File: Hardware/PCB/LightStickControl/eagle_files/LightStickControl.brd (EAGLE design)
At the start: 100 x 80 mm, 3 parts

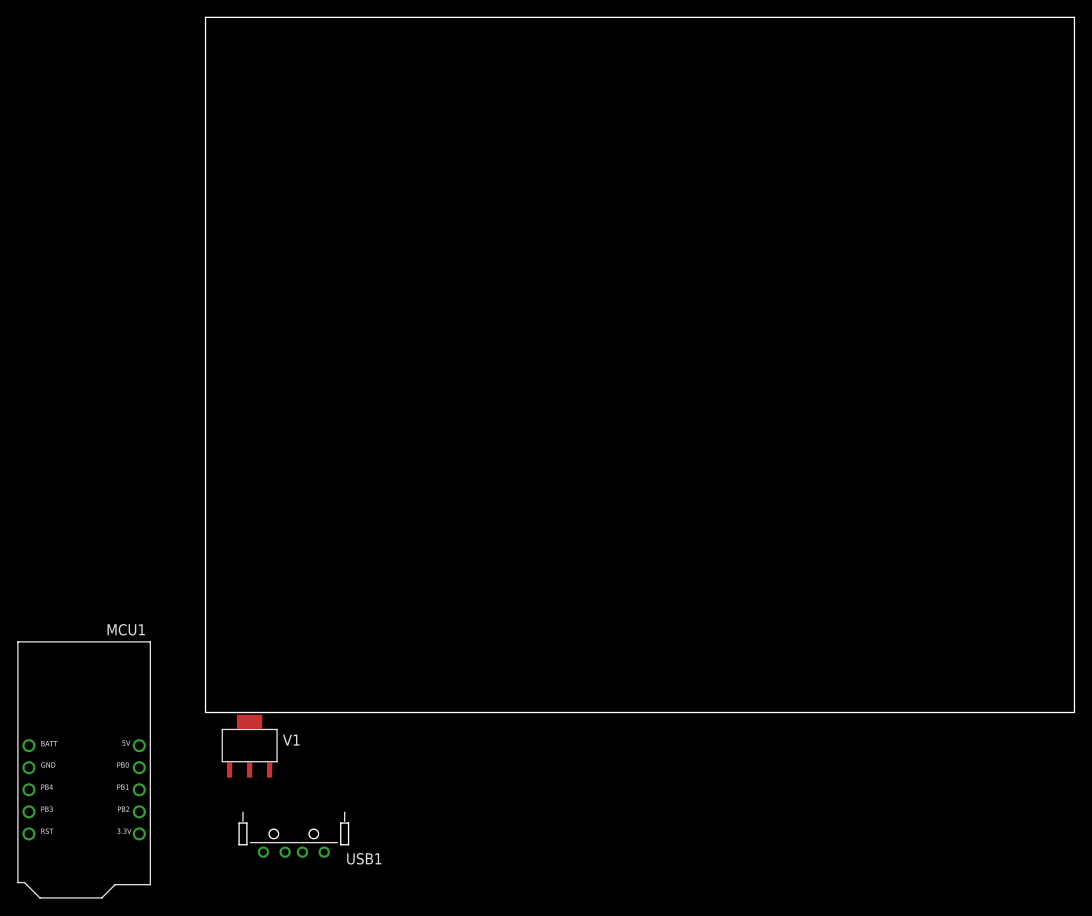
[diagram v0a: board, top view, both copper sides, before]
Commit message: First cut of board layout. Add connectors. Label everything.
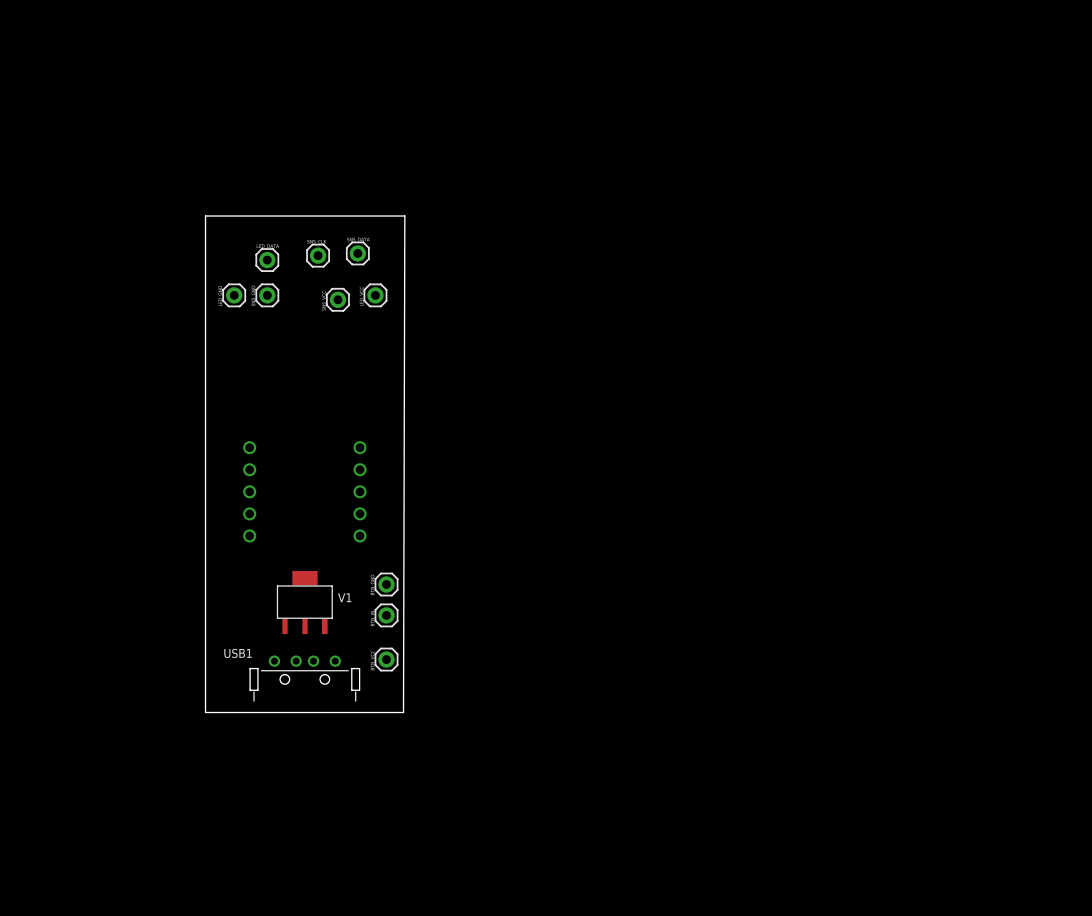
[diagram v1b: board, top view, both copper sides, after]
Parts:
- added BTN_GND, BTN_IN, BTN_VCC, LED_DATA, LED_GND, LED_VCC, SNS_CLK, SNS_DATA, SNS_GND, SNS_VCC: (no value), SparkFun-Connectors:1X01
- moved MCU1 42.7 mm to (11.4, 25.4), flipped to the bottom, turned to 180 degrees
- moved USB1 17.8 mm to (11.4, 3.81), turned to 180 degrees
- moved V1 17.7 mm to (11.4, 12.7)
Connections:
- removed net N$1: USB1.GND, V1.GND
- removed net N$2: USB1.VCC, V1.VIN
- removed net N$3: V1.VOUT2
- removed net N$4: USB1.D+, USB1.D-
- new net BTN_IN: BTN_IN.1, MCU1.PB3
- new net GND: BTN_GND.1, LED_GND.1, MCU1.GND, SNS_GND.1, USB1.D+, USB1.D-, USB1.GND, V1.GND
- new net LED_DATA: LED_DATA.1, MCU1.PB4
- new net LED_VCC: LED_VCC.1, V1.VOUT2
- new net SNS_CLK: MCU1.PB2, SNS_CLK.1
- new net SNS_DATA: MCU1.PB0, SNS_DATA.1
- new net SNS_VCC: BTN_VCC.1, MCU1.3.3V, SNS_VCC.1
- new net VCC_IN: MCU1.BATT, USB1.VCC, V1.VIN
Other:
- board size 100 x 80 mm -> 22.9 x 57.1 mm

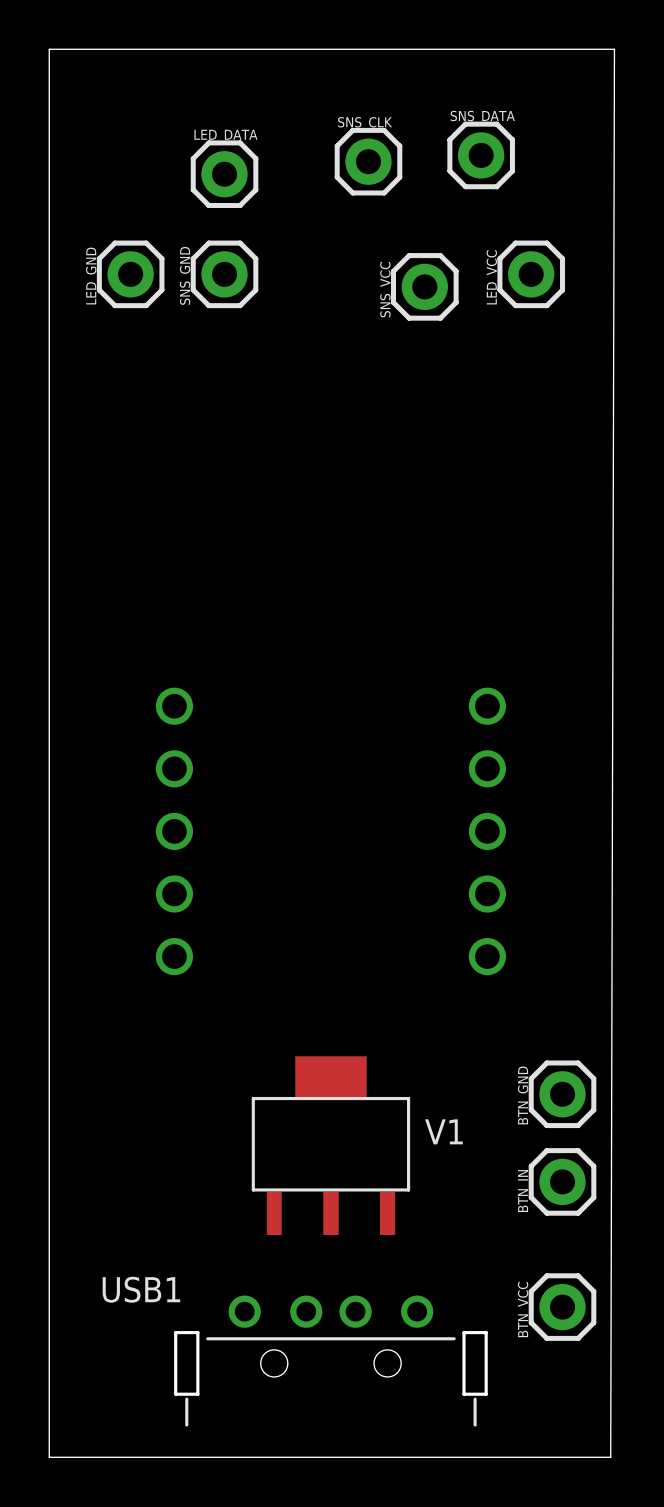
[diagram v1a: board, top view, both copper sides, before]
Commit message: Add support components and lay initial placement.
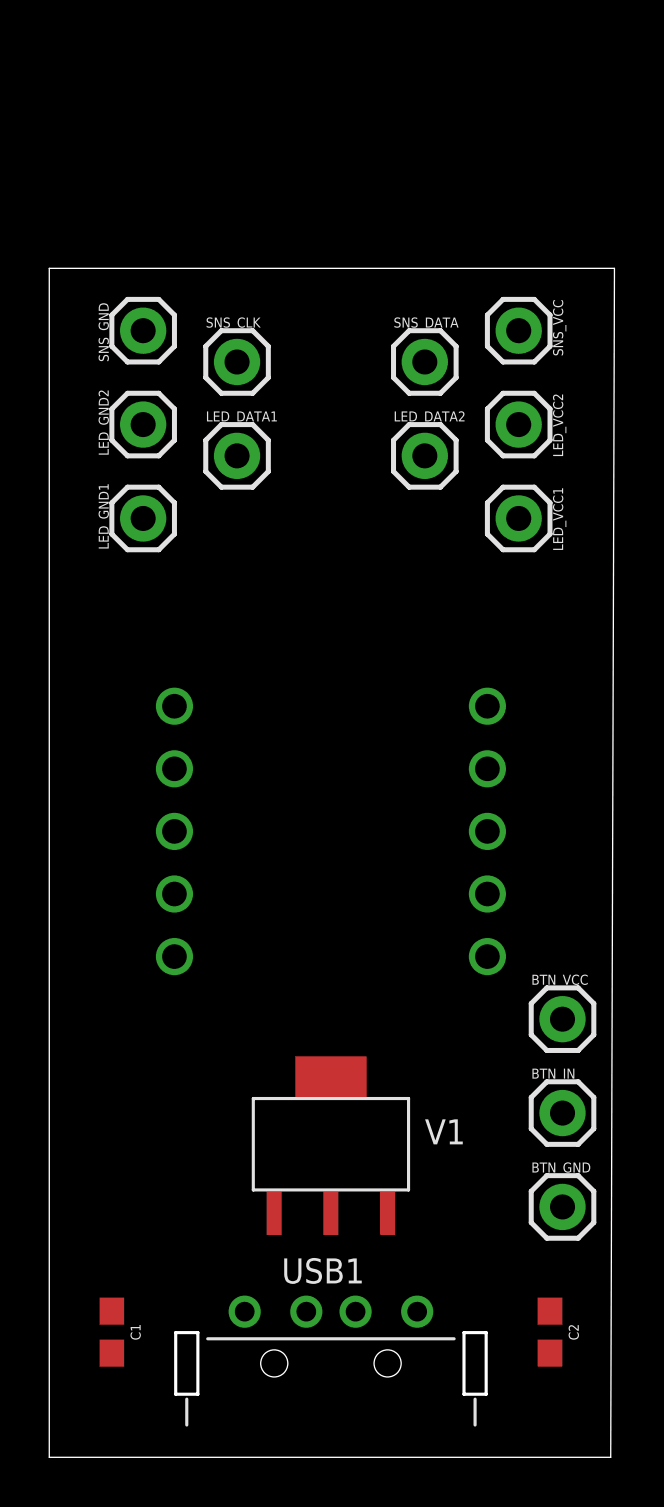
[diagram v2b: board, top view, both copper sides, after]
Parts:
- removed LED_DATA, LED_GND, LED_VCC: (no value), SparkFun-Connectors:1X01
- added C1, C2: 4.7uF, SparkFun-Capacitors:0603
- added LED_DATA1, LED_DATA2, LED_GND1, LED_GND2, LED_VCC1, LED_VCC2: (no value), SparkFun-Connectors:1X01
- moved BTN_VCC 11.7 mm to (20.8, 17.8), turned to 0 degrees
- moved SNS_CLK 9.72 mm to (7.62, 44.5)
- moved SNS_DATA 8.69 mm to (15.2, 44.5)
- moved BTN_GND 4.57 mm to (20.8, 10.2), turned to 0 degrees
- moved SNS_VCC 4.20 mm to (19.1, 45.7), turned to 270 degrees
- moved SNS_GND 4.02 mm to (3.81, 45.7)
- moved BTN_IN 2.79 mm to (20.8, 14.0), turned to 0 degrees
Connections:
- net GND: now also C1.2, C2.2, LED_GND1.1, LED_GND2.1; no longer LED_GND.1
- net LED_DATA: now also LED_DATA1.1, LED_DATA2.1; no longer LED_DATA.1
- net LED_VCC: now also C2.1, LED_VCC1.1, LED_VCC2.1; no longer LED_VCC.1
- net VCC_IN: now also C1.1
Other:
- board size 22.9 x 57.1 mm -> 22.9 x 48.2 mm

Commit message: Added routing.
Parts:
- moved LED_GND2 15.2 mm to (19.1, 41.9), turned to 270 degrees
- moved LED_VCC2 15.2 mm to (3.81, 41.9), turned to 90 degrees
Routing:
- net GND: track 0.00 -> 102.9 mm
- net LED_VCC: track 0.00 -> 60.4 mm, vias 0 -> 1
- net VCC_IN: track 0.00 -> 39.9 mm
- net SNS_VCC: track 0.00 -> 31.8 mm
- net SNS_DATA: track 0.00 -> 25.4 mm
- net LED_DATA: track 0.00 -> 25.3 mm
- net BTN_IN: track 0.00 -> 25.1 mm
- net SNS_CLK: track 0.00 -> 22.8 mm, vias 0 -> 1
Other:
- board text added: "LightStickControl 3/8/2017 F. Lee"

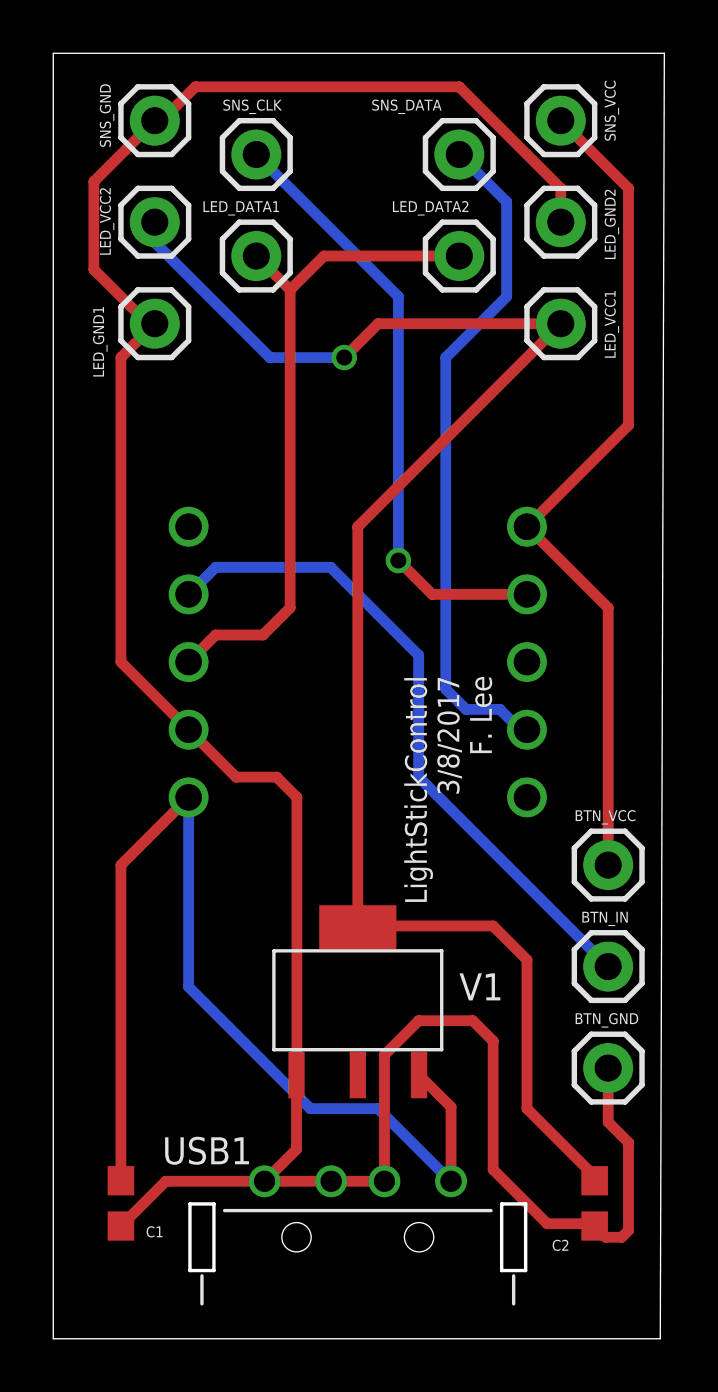
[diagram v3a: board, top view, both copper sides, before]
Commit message: Shorten PCB to allow for a snug fit for the USB plug A
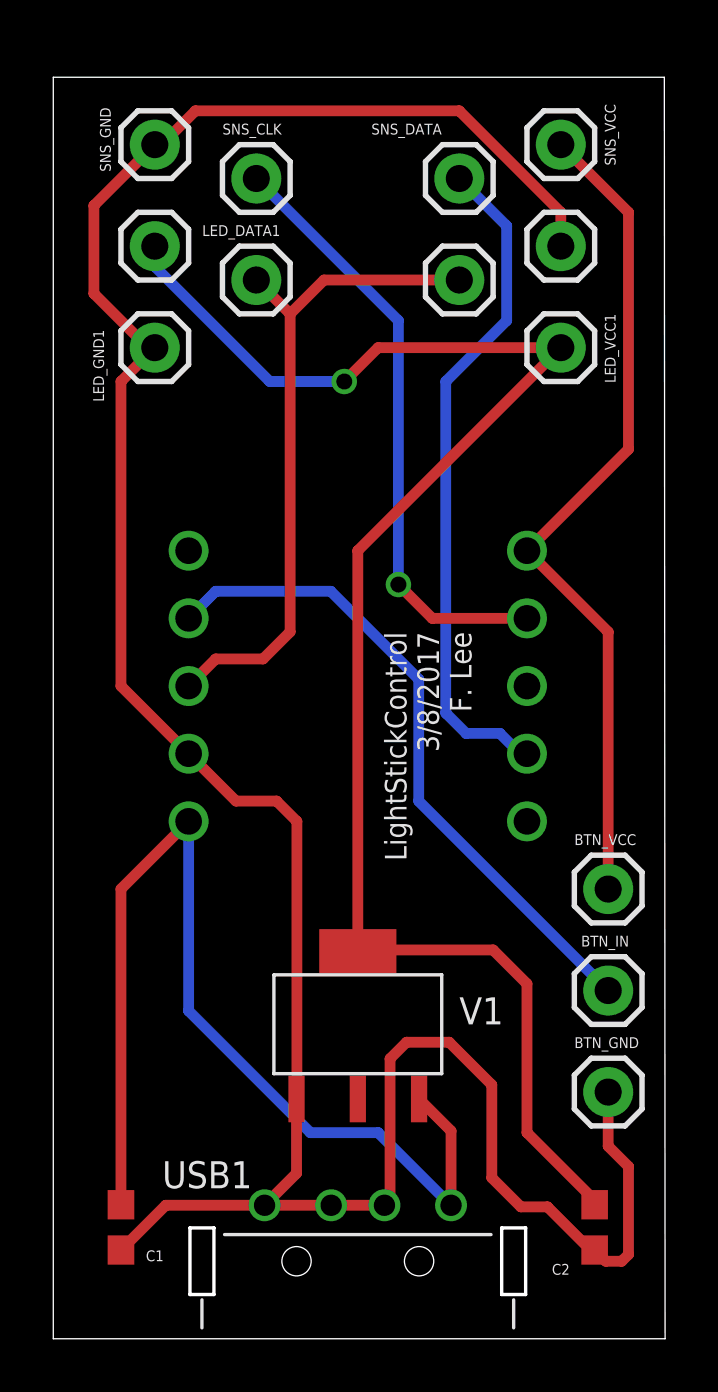
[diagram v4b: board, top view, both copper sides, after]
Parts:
- moved SNS_CLK 0.90 mm to (7.62, 43.5)
- moved SNS_DATA 0.90 mm to (15.2, 43.5)
- moved BTN_VCC 0.90 mm to (20.8, 16.9)
- moved BTN_GND 0.90 mm to (20.8, 9.26)
- moved BTN_IN 0.90 mm to (20.8, 13.1)
- moved C1 0.90 mm to (2.54, 4.18)
- moved C2 0.90 mm to (20.3, 4.18)
- moved USB1 0.90 mm to (11.4, 2.91)
- moved LED_DATA1 0.90 mm to (7.62, 39.7)
- moved LED_DATA2 0.90 mm to (15.2, 39.7)
- moved LED_GND1 0.90 mm to (3.81, 37.2)
- moved LED_GND2 0.90 mm to (19.1, 41.0)
- moved LED_VCC1 0.90 mm to (19.1, 37.2)
- moved LED_VCC2 0.90 mm to (3.81, 41.0)
- moved MCU1 0.90 mm to (11.4, 24.5)
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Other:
- board size 22.9 x 48.2 mm -> 23 x 47.4 mm

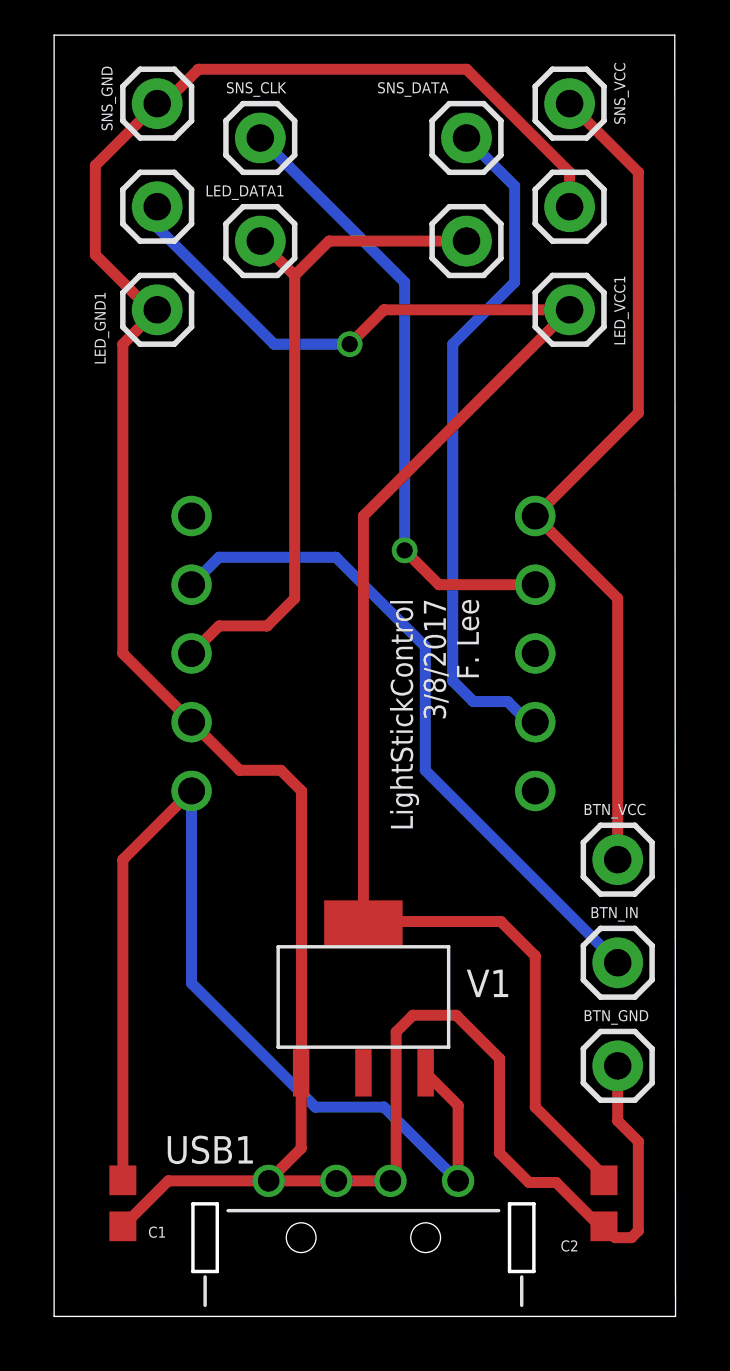
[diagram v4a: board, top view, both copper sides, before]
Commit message: Add new switching voltage regulator.
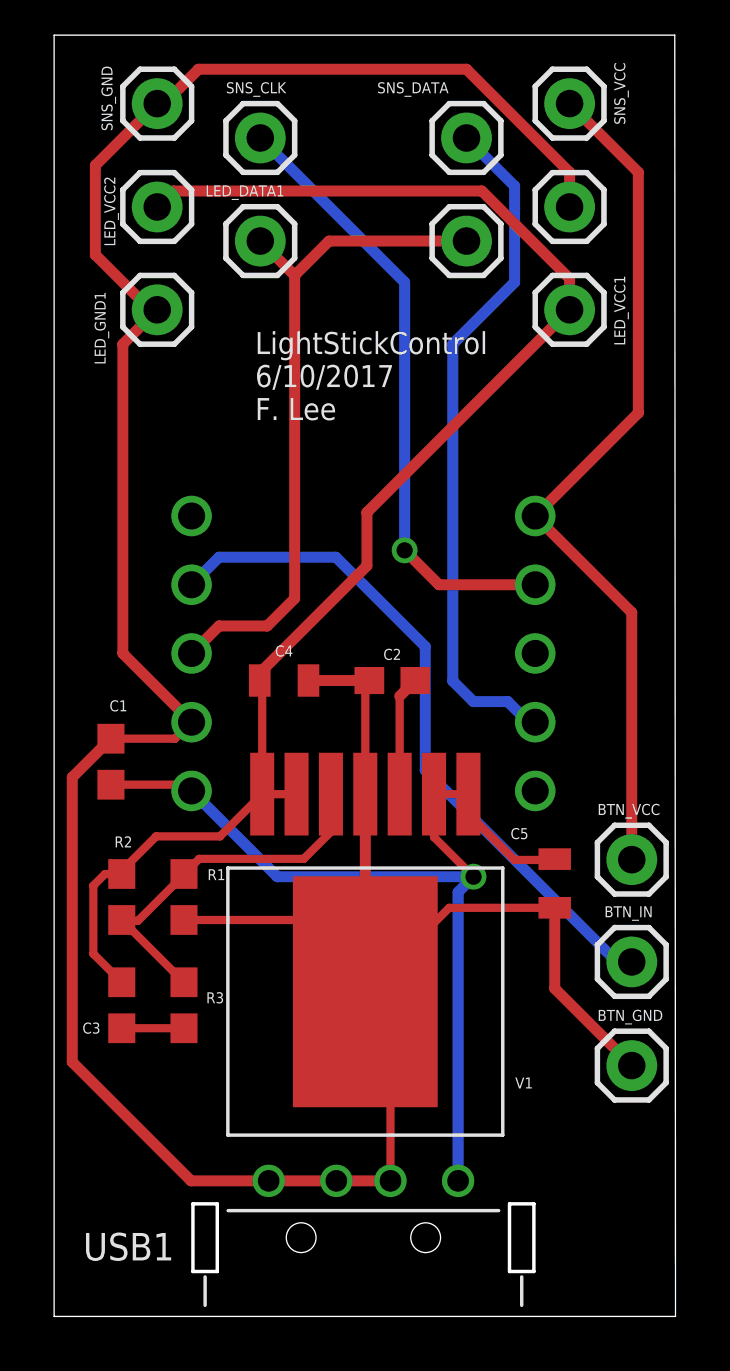
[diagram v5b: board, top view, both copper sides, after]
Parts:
- added C3: 100pF, SparkFun-Capacitors:0603
- added C4: 47uF, SparkFun-Capacitors:0805
- added C5: 22uF, SparkFun-Capacitors:0805
- added R1: 33k, SparkFun-Resistors:0603
- added R2: 100k, SparkFun-Resistors:0603
- added R3: 4.53k, SparkFun-Resistors:0603
- C2: value 4.7uF -> 10nF
- V1: value VOLTAGE_REGULATOR_AP2114H -> LMZ10503; device freddyLibr:SOT-223 -> freddyLibr:TO-PMOD
- moved C2 20.8 mm to (12.5, 23.5), turned to 0 degrees
- moved C1 16.3 mm to (2.10, 20.5), turned to 90 degrees
- moved BTN_IN 0.52 mm to (21.3, 13.1)
- moved BTN_GND 0.52 mm to (21.3, 9.27)
- moved BTN_VCC 0.52 mm to (21.3, 16.9)
- moved V1 0.21 mm to (11.5, 12.0), turned to 180 degrees
- turned LED_VCC2 to 0 degrees
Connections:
- removed net LED_VCC: C2.1, LED_VCC1.1, LED_VCC2.1, V1.VOUT2
- new net FB: R1.2, R2.1, R3.2, V1.FB
- new net SS: C2.2, V1.SS
- new net VOUT: C3.2, C4.1, LED_VCC1.1, LED_VCC2.1, R2.2, V1.VOUT1, V1.VOUT2
- new net VOUT_C: C3.1, R3.1
- net GND: now also C2.1, C4.2, C5.2, R1.1, V1.GND_PAD; no longer C2.2
- net VCC_IN: now also C5.1, V1.EN
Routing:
- net LED_VCC: track 60.4 -> 0.00 mm, vias 1 -> 0
- net VOUT: track 0.00 -> 53.6 mm
- net GND: track 102.5 -> 117.5 mm
- net FB: track 0.00 -> 13.8 mm
- net SS: track 0.00 -> 4.44 mm
- net VCC_IN: track 39.9 -> 35.8 mm, vias 0 -> 1
- net VOUT_C: track 0.00 -> 2.30 mm
- net BTN_IN: track 25.1 -> 25.6 mm
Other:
- board text added: "LightStickControl 6/10/2017 F. Lee"
- board text removed: "LightStickControl 3/8/2017 F. Lee"
